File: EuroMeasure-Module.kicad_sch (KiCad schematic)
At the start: 0 parts

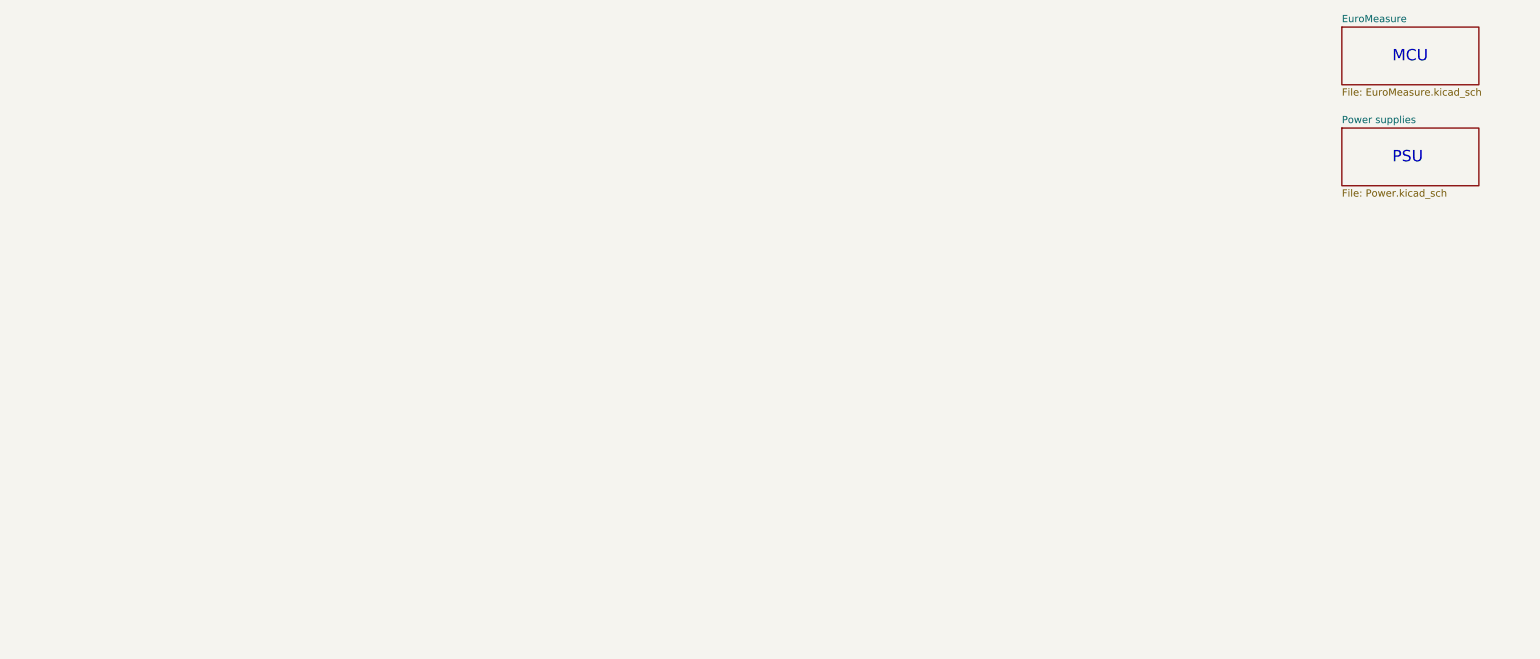
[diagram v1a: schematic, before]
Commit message: Converted for use as the single EuroMeasure.sch file
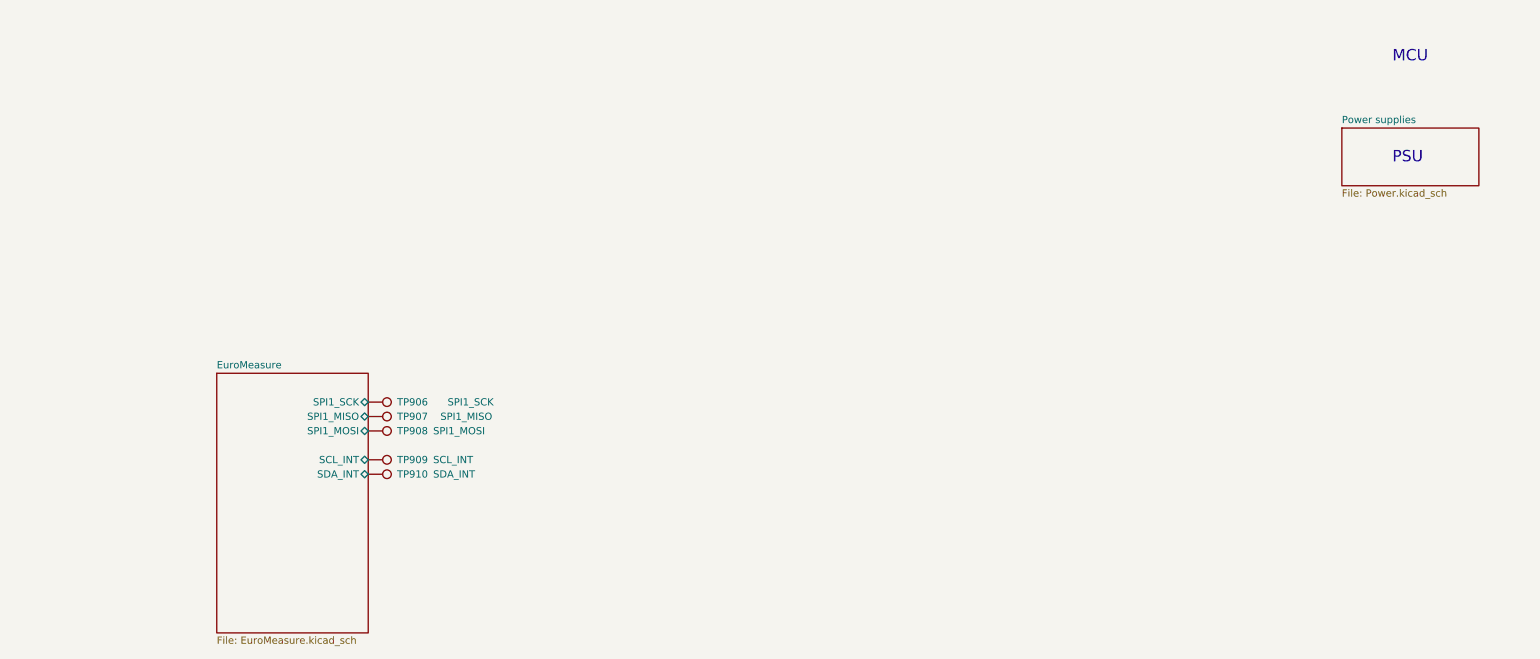
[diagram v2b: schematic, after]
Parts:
- added TP906: SPI1_SCK, MEMS_Custom:TestPoint_Pad_D1.0mm, symbol Connector:TestPoint
- added TP907: SPI1_MISO, MEMS_Custom:TestPoint_Pad_D1.0mm, symbol Connector:TestPoint
- added TP908: SPI1_MOSI, MEMS_Custom:TestPoint_Pad_D1.0mm, symbol Connector:TestPoint
- added TP909: SCL_INT, MEMS_Custom:TestPoint_Pad_D1.0mm, symbol Connector:TestPoint
- added TP910: SDA_INT, MEMS_Custom:TestPoint_Pad_D1.0mm, symbol Connector:TestPoint
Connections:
- new net EuroMeasure/SCL_INT: TP909.1
- new net EuroMeasure/SDA_INT: TP910.1
- new net EuroMeasure/SPI1_MISO: TP907.1
- new net EuroMeasure/SPI1_MOSI: TP908.1
- new net EuroMeasure/SPI1_SCK: TP906.1
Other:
- sheet EuroMeasure ports: added SCL_INT, SDA_INT, SPI1_MISO, SPI1_MOSI, SPI1_SCK; removed none
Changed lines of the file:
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@@
     (effects (font (size 2 2)) (justify left bottom))
   )
-  (sheet (at 254 19.05) (size 24.13 10.16) (fields_autoplaced)
-    (stroke (width 0.1524) (type solid))
-    (fill (color 0 0 0 0.0000))
-    (property "Sheetname" "EuroMeasure" (at 254 18.3384 0)
-      (effects (font (size 1.27 1.27)) (justify left bottom))
-    )
-    (property "Sheetfile" "EuroMeasure.kicad_sch" (at 254 29.7946 0)
-      (effects (font (size 1.27 1.27)) (justify left top))
-    )
-    (instances
-      (project "EuroMeasure-Module"
-        (path "/9c84a828-ebcc-4f88-b5cc-11be4f5044ad" (page "2"))
+  (symbol (lib_id "Connector:TestPoint") (at 82.55 95.25 270) (unit 1)
+    (in_bom yes) (on_board yes) (dnp no)
+    (property "Reference" "TP909" (at 87.63 95.25 90)
+      (effects (font (size 1.27 1.27)) (justify left))
+    )
+    (property "Value" "SCL_INT" (at 93.98 95.25 90)
+      (effects (font (size 1.27 1.27)) (justify left))
+    )
+    (property "Footprint" "MEMS_Custom:TestPoint_Pad_D1.0mm" (at 82.55 100.33 0)
+      (effects (font (size 1.27 1.27)) hide)
+    )
+    (property "Datasheet" "~" (at 82.55 100.33 0)
+      (effects (font (size 1.27 1.27)) hide)
+    )
+    (pin "1")
+    (instances
+      (project "EuroMeasure-Module"
+        (path "/9c84a828-ebcc-4f88-b5cc-11be4f5044ad/abf38db6-df21-42a4-a2d8-4fd7d247b99e"
+          (reference "TP909") (unit 1)
+        )
+        (path "/9c84a828-ebcc-4f88-b5cc-11be4f5044ad"
+          (reference "TP909") (unit 1)
+        )
+      )
+      (project "EuroMeasure-Generator"
+        (path "/c0f57af1-51e3-4b1b-8afb-67a4c2f2a5dd/496cddf1-5099-4e86-bf70-be84b3dd55bc"
+          (reference "TP909") (unit 1)
+        )
+        (path "/c0f57af1-51e3-4b1b-8afb-67a4c2f2a5dd/5c32201f-9cee-4b13-85be-b08d669b436d"
+          (reference "TP909") (unit 1)
+        )
+      )
+    )
+  )
+  (symbol (lib_id "Connector:TestPoint") (at 82.55 90.17 270) (mirror x) (unit 1)
+    (in_bom yes) (on_board yes) (dnp no)
+    (property "Reference" "TP908" (at 87.63 90.17 90)
+      (effects (font (size 1.27 1.27)) (justify left))
+    )
+    (property "Value" "SPI1_MOSI" (at 93.98 90.17 90)
+      (effects (font (size 1.27 1.27)) (justify left))
+    )
+    (property "Footprint" "MEMS_Custom:TestPoint_Pad_D1.0mm" (at 82.55 85.09 0)
+      (effects (font (size 1.27 1.27)) hide)
+    )
+    (property "Datasheet" "~" (at 82.55 85.09 0)
+      (effects (font (size 1.27 1.27)) hide)
+    )
+    (pin "1")
+    (instances
+      (project "EuroMeasure-Module"
+        (path "/9c84a828-ebcc-4f88-b5cc-11be4f5044ad/abf38db6-df21-42a4-a2d8-4fd7d247b99e"
+          (reference "TP908") (unit 1)
+        )
+        (path "/9c84a828-ebcc-4f88-b5cc-11be4f5044ad"
+          (reference "TP908") (unit 1)
+        )
+      )
+      (project "EuroMeasure-Generator"
+        (path "/c0f57af1-51e3-4b1b-8afb-67a4c2f2a5dd/496cddf1-5099-4e86-bf70-be84b3dd55bc"
+          (reference "TP908") (unit 1)
+        )
+        (path "/c0f57af1-51e3-4b1b-8afb-67a4c2f2a5dd/5c32201f-9cee-4b13-85be-b08d669b436d"
+          (reference "TP908") (unit 1)
+        )
+      )
+    )
+  )
+  (symbol (lib_id "Connector:TestPoint") (at 82.55 97.79 270) (mirror x) (unit 1)
+    (in_bom yes) (on_board yes) (dnp no)
+    (property "Reference" "TP910" (at 87.63 97.79 90)
+      (effects (font (size 1.27 1.27)) (justify left))
+    )
+    (property "Value" "SDA_INT" (at 93.98 97.79 90)
+      (effects (font (size 1.27 1.27)) (justify left))
+    )
+    (property "Footprint" "MEMS_Custom:TestPoint_Pad_D1.0mm" (at 82.55 92.71 0)
+      (effects (font (size 1.27 1.27)) hide)
+    )
+    (property "Datasheet" "~" (at 82.55 92.71 0)
+      (effects (font (size 1.27 1.27)) hide)
+    )
+    (pin "1")
+    (instances
+      (project "EuroMeasure-Module"
+        (path "/9c84a828-ebcc-4f88-b5cc-11be4f5044ad/abf38db6-df21-42a4-a2d8-4fd7d247b99e"
+          (reference "TP910") (unit 1)
+        )
+        (path "/9c84a828-ebcc-4f88-b5cc-11be4f5044ad"
+          (reference "TP910") (unit 1)
+        )
+      )
+      (project "EuroMeasure-Generator"
+        (path "/c0f57af1-51e3-4b1b-8afb-67a4c2f2a5dd/496cddf1-5099-4e86-bf70-be84b3dd55bc"
+          (reference "TP910") (unit 1)
+        )
+        (path "/c0f57af1-51e3-4b1b-8afb-67a4c2f2a5dd/5c32201f-9cee-4b13-85be-b08d669b436d"
+          (reference "TP910") (unit 1)
+        )
+      )
+    )
+  )
+  (symbol (lib_id "Connector:TestPoint") (at 82.55 85.09 270) (unit 1)
+    (in_bom yes) (on_board yes) (dnp no)
+    (property "Reference" "TP906" (at 87.63 85.09 90)
+      (effects (font (size 1.27 1.27)) (justify left))
+    )
+    (property "Value" "SPI1_SCK" (at 96.52 85.09 90)
+      (effects (font (size 1.27 1.27)) (justify left))
+    )
+    (property "Footprint" "MEMS_Custom:TestPoint_Pad_D1.0mm" (at 82.55 90.17 0)
+      (effects (font (size 1.27 1.27)) hide)
+    )
+    (property "Datasheet" "~" (at 82.55 90.17 0)
+      (effects (font (size 1.27 1.27)) hide)
+    )
+    (pin "1")
+    (instances
+      (project "EuroMeasure-Module"
+        (path "/9c84a828-ebcc-4f88-b5cc-11be4f5044ad/abf38db6-df21-42a4-a2d8-4fd7d247b99e"
+          (reference "TP906") (unit 1)
+        )
+        (path "/9c84a828-ebcc-4f88-b5cc-11be4f5044ad"
+          (reference "TP906") (unit 1)
+        )
+      )
+      (project "EuroMeasure-Generator"
+        (path "/c0f57af1-51e3-4b1b-8afb-67a4c2f2a5dd/496cddf1-5099-4e86-bf70-be84b3dd55bc"
+          (reference "TP906") (unit 1)
+        )
+        (path "/c0f57af1-51e3-4b1b-8afb-67a4c2f2a5dd/5c32201f-9cee-4b13-85be-b08d669b436d"
+          (reference "TP906") (unit 1)
+        )
+      )
+    )
+  )
+  (symbol (lib_id "Connector:TestPoint") (at 82.55 87.63 270) (mirror x) (unit 1)
+    (in_bom yes) (on_board yes) (dnp no)
+    (property "Reference" "TP907" (at 87.63 87.63 90)
+      (effects (font (size 1.27 1.27)) (justify left))
+    )
+    (property "Value" "SPI1_MISO" (at 95.25 87.63 90)
+      (effects (font (size 1.27 1.27)) (justify left))
+    )
+    (property "Footprint" "MEMS_Custom:TestPoint_Pad_D1.0mm" (at 82.55 82.55 0)
+      (effects (font (size 1.27 1.27)) hide)
+    )
+    (property "Datasheet" "~" (at 82.55 82.55 0)
+      (effects (font (size 1.27 1.27)) hide)
+    )
+    (pin "1")
+    (instances
+      (project "EuroMeasure-Module"
+        (path "/9c84a828-ebcc-4f88-b5cc-11be4f5044ad/abf38db6-df21-42a4-a2d8-4fd7d247b99e"
+          (reference "TP907") (unit 1)
+        )
+        (path "/9c84a828-ebcc-4f88-b5cc-11be4f5044ad"
+          (reference "TP907") (unit 1)
+        )
+      )
+      (project "EuroMeasure-Generator"
+        (path "/c0f57af1-51e3-4b1b-8afb-67a4c2f2a5dd/496cddf1-5099-4e86-bf70-be84b3dd55bc"
+          (reference "TP907") (unit 1)
+        )
+        (path "/c0f57af1-51e3-4b1b-8afb-67a4c2f2a5dd/5c32201f-9cee-4b13-85be-b08d669b436d"
+          (reference "TP907") (unit 1)
+        )
       )
     )
@@
       )
     )
+  )
+  (sheet (at 55.88 80.01) (size 26.67 45.72) (fields_autoplaced)
+    (stroke (width 0.1524) (type solid))
+    (fill (color 0 0 0 0.0000))
+    (property "Sheetname" "EuroMeasure" (at 55.88 79.2984 0)
+      (effects (font (size 1.27 1.27)) (justify left bottom))
+    )
+    (property "Sheetfile" "EuroMeasure.kicad_sch" (at 55.88 126.3146 0)
+      (effects (font (size 1.27 1.27)) (justify left top))
+    )
+    (pin "SPI1_SCK" bidirectional (at 82.55 85.09 0)
+      (effects (font (size 1.27 1.27)) (justify right))
+    )
+    (pin "SDA_INT" bidirectional (at 82.55 97.79 0)
+      (effects (font (size 1.27 1.27)) (justify right))
+    )
+    (pin "SCL_INT" bidirectional (at 82.55 95.25 0)
+      (effects (font (size 1.27 1.27)) (justify right))
+    )
+    (pin "SPI1_MOSI" bidirectional (at 82.55 90.17 0)
+      (effects (font (size 1.27 1.27)) (justify right))
+    )
+    (pin "SPI1_MISO" bidirectional (at 82.55 87.63 0)
+      (effects (font (size 1.27 1.27)) (justify right))
+    )
+    (instances
+      (project "EuroMeasure-Module"
+        (path "/9c84a828-ebcc-4f88-b5cc-11be4f5044ad" (page "3"))
+      )
+    )

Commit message: Cleaned up schematic
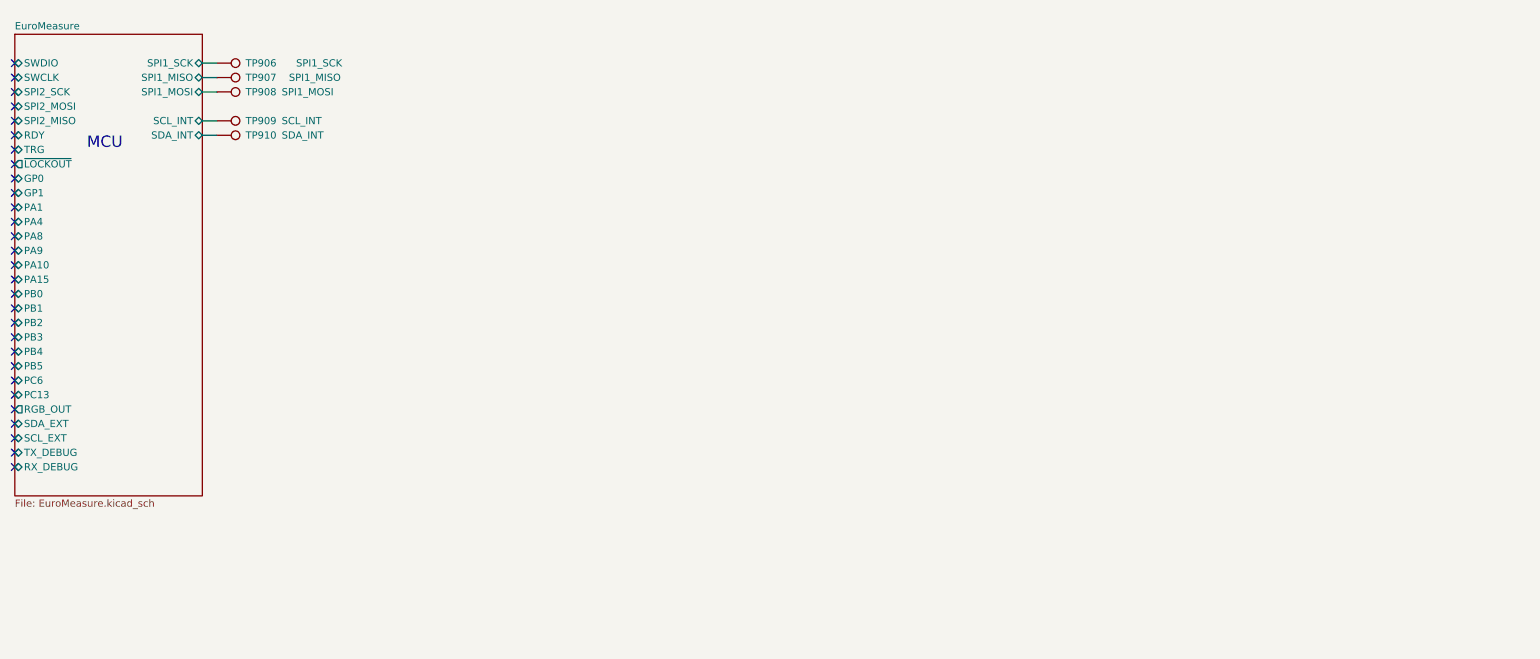
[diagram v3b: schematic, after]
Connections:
- no-connect marks 0 -> 29
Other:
- removed sheet Power supplies
- sheet EuroMeasure ports: added GP0, GP1, PA1, PA10, PA15, PA4, PA8, PA9, PB0, PB1, PB2, PB3, PB4, PB5, PC13, PC6, RDY, RGB_OUT, RX_DEBUG, SCL_EXT, SDA_EXT, SPI2_MISO, SPI2_MOSI, SPI2_SCK, SWCLK, SWDIO, TRG, TX_DEBUG, ~{LOCKOUT}; removed none
- note removed: "PSU"
- moved on the sheet: TP906, TP907, TP908, TP909, TP910

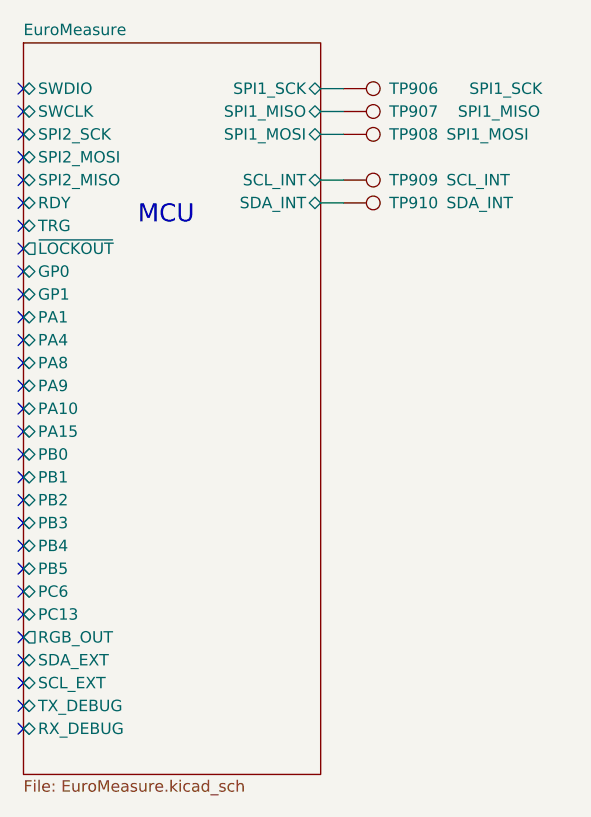
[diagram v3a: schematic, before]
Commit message: Revised sheet path
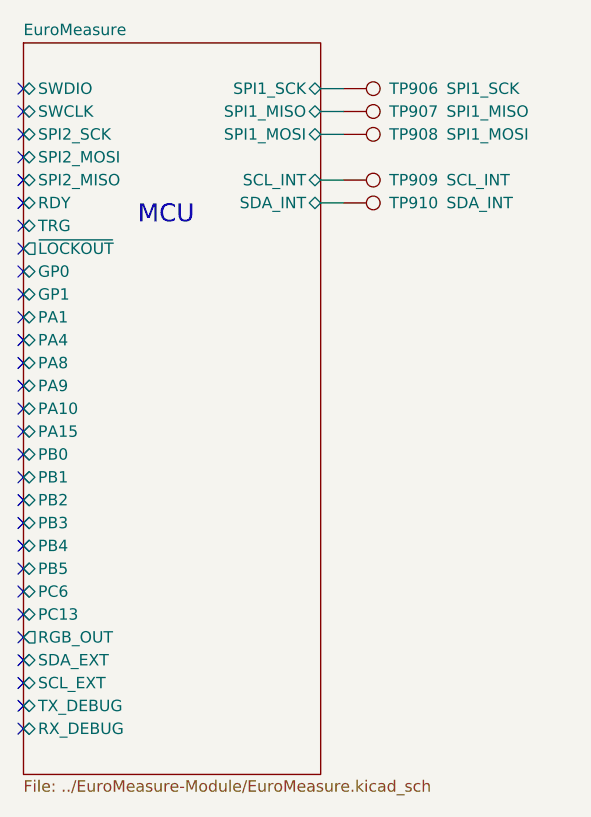
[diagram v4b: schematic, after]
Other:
- sheet EuroMeasure: file EuroMeasure.kicad_sch -> ../EuroMeasure-Module/EuroMeasure.kicad_sch
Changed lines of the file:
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@@
       (effects (font (size 1.27 1.27)) (justify left))
     )
-    (property "Value" "SPI1_SCK" (at 69.85 25.4 90)
+    (property "Value" "SPI1_SCK" (at 67.31 25.4 90)
       (effects (font (size 1.27 1.27)) (justify left))
     )
@@
       (effects (font (size 1.27 1.27)) (justify left))
     )
-    (property "Value" "SPI1_MISO" (at 68.58 27.94 90)
+    (property "Value" "SPI1_MISO" (at 67.31 27.94 90)
       (effects (font (size 1.27 1.27)) (justify left))
     )
@@
       (effects (font (size 1.27 1.27)) (justify left bottom))
     )
-    (property "Sheetfile" "EuroMeasure.kicad_sch" (at 20.32 102.1846 0)
+    (property "Sheetfile" "../EuroMeasure-Module/EuroMeasure.kicad_sch" (at 20.32 102.1846 0)
       (effects (font (size 1.27 1.27)) (justify left top))
     )

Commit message: Edited visibility in bom
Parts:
- TP906, TP907, TP908, TP909, TP910: symbol Connector:TestPoint -> MEMS_Electromechanical:TestPoint; now left out of the parts list
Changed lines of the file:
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@@
     (effects (font (size 2 2)) (justify left bottom))
   )
-  (symbol (lib_id "Connector:TestPoint") (at 55.88 35.56 270) (unit 1)
-    (in_bom yes) (on_board yes) (dnp no)
+  (symbol (lib_id "MEMS_Electromechanical:TestPoint") (at 55.88 35.56 270) (unit 1)
+    (in_bom no) (on_board yes) (dnp no)
     (property "Reference" "TP909" (at 60.96 35.56 90)
       (effects (font (size 1.27 1.27)) (justify left))
@@
     )
   )
-  (symbol (lib_id "Connector:TestPoint") (at 55.88 30.48 270) (mirror x) (unit 1)
-    (in_bom yes) (on_board yes) (dnp no)
+  (symbol (lib_id "MEMS_Electromechanical:TestPoint") (at 55.88 30.48 270) (mirror x) (unit 1)
+    (in_bom no) (on_board yes) (dnp no)
     (property "Reference" "TP908" (at 60.96 30.48 90)
       (effects (font (size 1.27 1.27)) (justify left))
@@
     )
   )
-  (symbol (lib_id "Connector:TestPoint") (at 55.88 38.1 270) (mirror x) (unit 1)
-    (in_bom yes) (on_board yes) (dnp no)
+  (symbol (lib_id "MEMS_Electromechanical:TestPoint") (at 55.88 38.1 270) (mirror x) (unit 1)
+    (in_bom no) (on_board yes) (dnp no)
     (property "Reference" "TP910" (at 60.96 38.1 90)
       (effects (font (size 1.27 1.27)) (justify left))
@@
     )
   )
-  (symbol (lib_id "Connector:TestPoint") (at 55.88 25.4 270) (unit 1)
-    (in_bom yes) (on_board yes) (dnp no)
+  (symbol (lib_id "MEMS_Electromechanical:TestPoint") (at 55.88 25.4 270) (unit 1)
+    (in_bom no) (on_board yes) (dnp no)
     (property "Reference" "TP906" (at 60.96 25.4 90)
       (effects (font (size 1.27 1.27)) (justify left))
@@
     )
   )
-  (symbol (lib_id "Connector:TestPoint") (at 55.88 27.94 270) (mirror x) (unit 1)
-    (in_bom yes) (on_board yes) (dnp no)
+  (symbol (lib_id "MEMS_Electromechanical:TestPoint") (at 55.88 27.94 270) (mirror x) (unit 1)
+    (in_bom no) (on_board yes) (dnp no)
     (property "Reference" "TP907" (at 60.96 27.94 90)
       (effects (font (size 1.27 1.27)) (justify left))
